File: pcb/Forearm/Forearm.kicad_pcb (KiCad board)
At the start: 4 copper layers, 64 x 64.1 mm, 11 parts, among them J1 Conn_01x02, J2 Conn_01x12_Ribbon_To_Top, J3 Conn_01x12_To_Bottom, U1 ESP32-S3-DEVKITC-1-N8R2, U2 4754

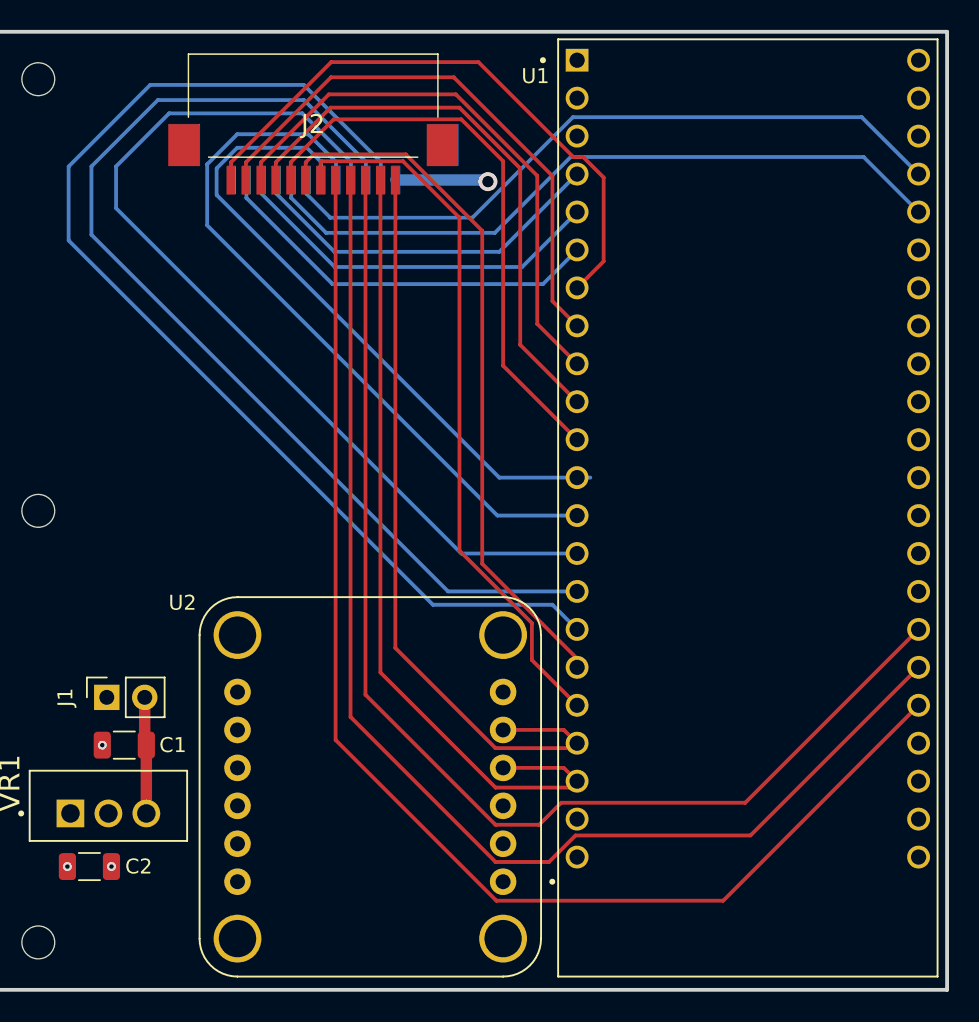
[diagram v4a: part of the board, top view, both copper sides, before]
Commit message: revised pcbs in preparation for pcb review; added pull-ups etc to forearm
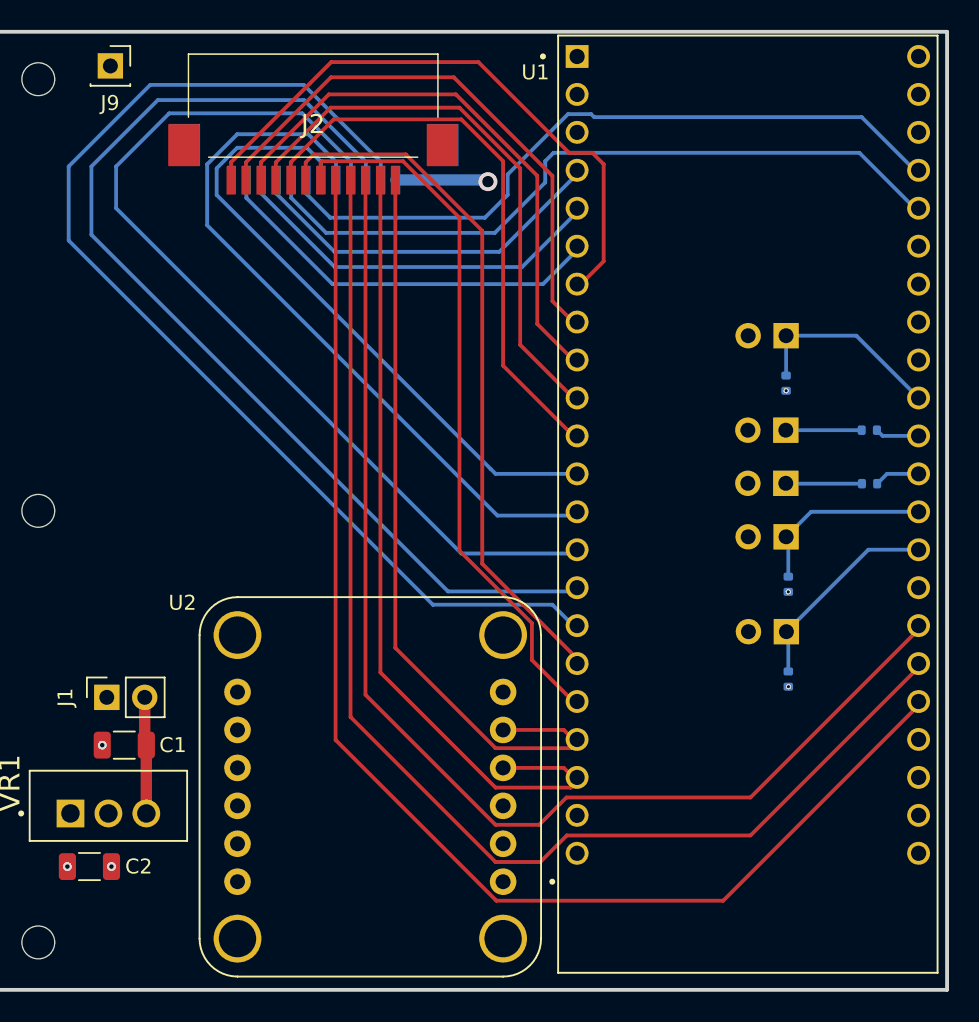
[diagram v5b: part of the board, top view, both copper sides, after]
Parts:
- added B0: Conn_01x02, Connector_PinSocket_2.54mm:PinSocket_1x02_P2.54mm_Vertical, B.Cu at (65.4, 57.9)
- added B1: Conn_01x02, Connector_PinSocket_2.54mm:PinSocket_1x02_P2.54mm_Vertical, B.Cu at (65.3, 51.6)
- added J9: Conn_01x01, Connector_PinSocket_2.54mm:PinSocket_1x01_P2.54mm_Vertical, F.Cu at (20.1, 20.1)
- added LED0: Conn_01x02, Connector_PinSocket_2.54mm:PinSocket_1x02_P2.54mm_Vertical, B.Cu at (65.3, 48.0)
- added LED1: Conn_01x02, Connector_PinSocket_2.54mm:PinSocket_1x02_P2.54mm_Vertical, B.Cu at (65.3, 44.4)
- added RB0: R, Resistor_SMD:R_0402_1005Metric, B.Cu at (65.5, 61.1)
- added RB1: R, Resistor_SMD:R_0402_1005Metric, B.Cu at (65.5, 54.7)
- added RLED0: R, Resistor_SMD:R_0402_1005Metric, B.Cu at (70.9, 48.0)
- added RLED1: R, Resistor_SMD:R_0402_1005Metric, B.Cu at (70.9, 44.4)
- added RS0: R, Resistor_SMD:R_0402_1005Metric, B.Cu at (65.3, 41.3)
- added S0: Conn_01x02, Connector_PinSocket_2.54mm:PinSocket_1x02_P2.54mm_Vertical, B.Cu at (65.3, 38.1)
- moved U1 0.25 mm to (62.8, 49.4)
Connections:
- U1 pad J3_10: BUTTON_0 -> SWITCH_0
- U1 pad J3_11: BUTTON_1 -> LED_1
- U1 pad J3_13: LED_1 -> BUTTON_1
- U1 pad J3_14: SWITCH_0 -> BUTTON_0
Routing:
- net BUTTON_0: track 0.00 -> 13.8 mm
- net SWITCH_0: track 0.00 -> 13.3 mm
- net BUTTON_1: track 0.00 -> 12.3 mm
- net Net-(LED0-Pin_1): track 0.00 -> 5.11 mm
- net Net-(LED1-Pin_1): track 0.00 -> 5.08 mm
- net LED_0: track 0.00 -> 3.05 mm
- net LED_1: track 0.00 -> 2.95 mm
- net SPOOLPOT_ADC1: track 47.8 -> 48.9 mm
- net HALL_S3: track 43.8 -> 42.8 mm
- net SPOOLPOT_ADC0: track 46.9 -> 47.9 mm
- net FEEDBACK_D4: track 40.3 -> 40.8 mm
- net 3V3: vias 2 -> 5

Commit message: re-work of pcbs for pin issues in progress 1
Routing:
- net GND: track 0.00 -> 3.64 mm, vias 2 -> 1
- net 3V3: track 6.22 -> 9.86 mm, vias 5 -> 4
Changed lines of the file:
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@@
 		(layer "Edge.Cuts")
+	)
+	(segment
+		(start 17.4291 73.4428)
+		(end 17.2241 73.6478)
+		(width 0.762)
+		(layer "F.Cu")
+		(net 1)
+	)
+	(segment
+		(start 17.4291 70.0918)
+		(end 17.4291 73.4428)
+		(width 0.762)
+		(layer "F.Cu")
+		(net 1)
 	)
 	(via
 		(at 19.5591 65.5198)
-		(size 0.6)
-		(drill 0.3)
-		(layers "F.Cu" "B.Cu")
-		(net 1)
-	)
-	(via
-		(at 17.2241 73.6478)
 		(size 0.6)
 		(drill 0.3)
@@
 		(layer "F.Cu")
 		(net 2)
+	)
+	(segment
+		(start 19.9691 73.4428)
+		(end 20.1741 73.6478)
+		(width 0.762)
+		(layer "F.Cu")
+		(net 3)
+	)
+	(segment
+		(start 19.9691 70.0918)
+		(end 19.9691 73.4428)
+		(width 0.762)
+		(layer "F.Cu")
+		(net 3)
 	)
 	(via
@@
 		(net 3)
 	)
-	(via
-		(at 20.1741 73.6478)
-		(size 0.6)
-		(drill 0.3)
-		(layers "F.Cu" "B.Cu")
-		(net 3)
-	)

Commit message: revised pcbs in prep for manufacture, rev2
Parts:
- J2: value Conn_01x12_Ribbon_To_Top -> Conn_01x16_Top; footprint 0522071233:0522071233 -> 522071633:CON_522071633_MOL
- J3: value Conn_01x12_To_Bottom -> Conn_01x16_Bottom; footprint 0522071233:0522071233 -> 522071633:CON_522071633_MOL
- moved B0 18.6 mm to (65.2, 39.4)
- moved RB0 18.6 mm to (65.3, 42.5)
- moved RLED1 11.4 mm to (70.8, 55.9)
- moved LED1 11.4 mm to (65.2, 55.9)
- moved J9 9.62 mm to (14.8, 28.1)
- moved RB1 5.75 mm to (65.3, 49.0)
- moved B1 5.74 mm to (65.2, 45.8)
- moved RS0 5.11 mm to (65.2, 36.2)
- moved S0 5.11 mm to (65.2, 33.0)
- moved LED0 4.19 mm to (65.2, 52.2)
- moved RLED0 4.19 mm to (70.8, 52.2)
- moved J3 2.95 mm to (31.6, 24.6)
- moved J2 2.95 mm to (31.6, 24.6)
- moved U1 0.23 mm to (62.7, 49.6)
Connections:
- J2 pad 1: IMU_SDA -> unconnected-(J2-Pin_1-Pad1)
- J2 pad 10: FEEDBACK_D2 -> HAPTIC_S1
- J2 pad 11: FEEDBACK_D3 -> HAPTIC_S0
- J2 pad 12: FEEDBACK_D4 -> FEEDBACK_D0
- J2 pad 2: IMU_SCL -> unconnected-(J2-Pin_2-Pad2)
- J2 pad 3: HAPTIC_S2 -> IMU_1_INT
- J2 pad 4: HAPTIC_S1 -> IMU_1_RST
- J2 pad 5: HAPTIC_S0 -> IMU_SDA
- J2 pad 6: HAPTIC_SCL -> IMU_SCL
- J2 pad 7: HAPTIC_SDA -> HAPTIC_SCL
- J2 pad 8: FEEDBACK_D0 -> HAPTIC_SDA
- J2 pad 9: FEEDBACK_D1 -> HAPTIC_S2
- J3 pad 1: FREE -> unconnected-(J3-Pin_1-Pad1)
- J3 pad 10: HALL_S0 -> SPOOLPOT_ADC0
- J3 pad 11: HALL_ADC -> HALL_S3
- J3 pad 12: 3V3 -> HALL_S2
- J3 pad 2: SPOOLPOT_ADC4 -> unconnected-(J3-Pin_2-Pad2)
- J3 pad 3: SPOOLPOT_ADC3 -> unconnected-(J3-Pin_3-Pad3)
- J3 pad 4: SPOOLPOT_ADC2 -> unconnected-(J3-Pin_4-Pad4)
- J3 pad 5: SPOOLPOT_ADC1 -> unconnected-(J3-Pin_5-Pad5)
- J3 pad 6: SPOOLPOT_ADC0 -> SPOOLPOT_ADC4
- J3 pad 7: HALL_S3 -> SPOOLPOT_ADC3
- J3 pad 8: HALL_S2 -> SPOOLPOT_ADC2
- J3 pad 9: HALL_S1 -> SPOOLPOT_ADC1
- U1 pad J1_17: HAPTIC_SDA -> HAPTIC_SCL
- U1 pad J1_18: HAPTIC_SCL -> HAPTIC_SDA
- U1 pad J1_19: IMU_SDA -> IMU_SCL
- U1 pad J1_20: IMU_SCL -> IMU_SDA
- U1 pad J3_11: LED_1 -> BUTTON_0
- U1 pad J3_12: LED_0 -> BUTTON_1
- U1 pad J3_13: BUTTON_1 -> HAPTIC_S2
- U1 pad J3_14: BUTTON_0 -> LED_0
- U1 pad J3_15: unconnected-(U1-GPIO45-PadJ3_15) -> LED_1
- U1 pad J3_16: HAPTIC_S2 -> unconnected-(U1-GPIO48-PadJ3_16)
- U1 pad J3_6: unconnected-(U1-MTMS/GPIO42-PadJ3_6) -> IMU_0_INT
- U1 pad J3_7: unconnected-(U1-MTDI/GPIO41-PadJ3_7) -> IMU_0_RST
- U1 pad J3_8: unconnected-(U1-MTDO/GPIO40-PadJ3_8) -> IMU_1_INT
- U1 pad J3_9: unconnected-(U1-MTCK/GPIO39-PadJ3_9) -> IMU_1_RST
- U2 pad JP1_6: unconnected-(U2-~{INT}-PadJP1_6) -> IMU_0_INT
- U2 pad JP2_1: unconnected-(U2-BT-PadJP2_1) -> IMU_0_RST
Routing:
- net IMU_0_RST: track 0.00 -> 110.5 mm
- net IMU_0_INT: track 0.00 -> 63.1 mm
- net IMU_1_RST: track 0.00 -> 54.8 mm
- net IMU_1_INT: track 0.00 -> 52.1 mm
- net IMU_SDA: track 51.7 -> 63.2 mm
- net HAPTIC_S2: track 80.5 -> 91.4 mm
- net HALL_S2: track 48.3 -> 57.4 mm
- net HALL_S3: track 42.8 -> 51.0 mm
- net HAPTIC_SCL: track 48.0 -> 40.6 mm
- net HAPTIC_S0: track 86.4 -> 93.6 mm
- net SWITCH_0: track 13.3 -> 18.6 mm
- net HALL_S1: track 63.0 -> 68.0 mm
- net FEEDBACK_D0: track 38.5 -> 42.6 mm
- net FEEDBACK_D1: track 38.0 -> 42.1 mm
- net FEEDBACK_D3: track 37.5 -> 41.5 mm
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
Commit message: pcbs for order, rev3
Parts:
- moved REF** 64.4 mm to (72.8, 78.7)
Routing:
- net GND: track 3.64 -> 9.10 mm, vias 1 -> 0
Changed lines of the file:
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@@
 	(footprint "MountingHole:MountingHole_2.2mm_M2"
 		(layer "F.Cu")
-		(at 15.2766 49.8348)
+		(at 72.8076 78.7258)
 		(descr "Mounting Hole 2.2mm, no annular, M2")
 		(tags "mounting hole 2.2mm no annular m2")
@@
 	)
 	(segment
+		(start 19.5591 65.5198)
+		(end 19.5591 67.9618)
+		(width 0.762)
+		(layer "F.Cu")
+		(net 1)
+	)
+	(segment
 		(start 17.4291 73.4428)
 		(end 17.2241 73.6478)
@@
 	)
 	(segment
-		(start 17.4291 70.0918)
-		(end 17.4291 73.4428)
+		(start 19.5591 67.9618)
+		(end 17.4291 70.0918)
 		(width 0.762)
 		(layer "F.Cu")
 		(net 1)
 	)
-	(via
-		(at 19.5591 65.5198)
-		(size 0.6)
-		(drill 0.3)
-		(layers "F.Cu" "B.Cu")
+	(segment
+		(start 17.4291 70.0918)
+		(end 17.4291 73.4428)
+		(width 0.762)
+		(layer "F.Cu")
 		(net 1)
 	)
@@
 	(via
 		(at 65.3146 49.5158)
-		(size 0.3556)
-		(drill 0.2032)
+		(size 0.4064)
+		(drill 0.3048)
 		(layers "F.Cu" "B.Cu")
 		(free yes)
@@
 	(via
 		(at 65.3254 43.0372)
-		(size 0.3556)
-		(drill 0.2032)
+		(size 0.4064)
+		(drill 0.3048)
 		(layers "F.Cu" "B.Cu")
 		(free yes)
@@
 	(via
 		(at 65.193 36.6892)
-		(size 0.3556)
-		(drill 0.2032)
+		(size 0.4064)
+		(drill 0.3048)
 		(layers "F.Cu" "B.Cu")
 		(free yes)
